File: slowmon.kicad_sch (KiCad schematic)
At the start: 20 parts, among them J801 20021121-00020C4LF, J802 20021121-00020C4LF

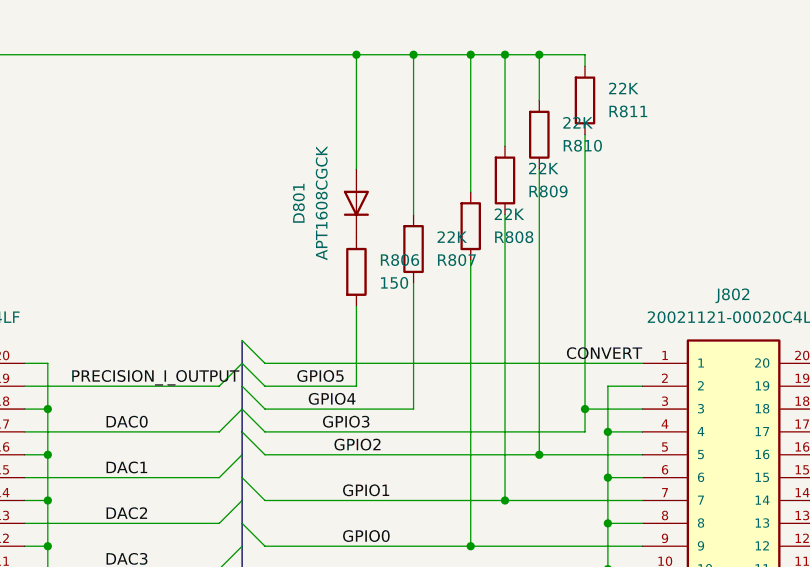
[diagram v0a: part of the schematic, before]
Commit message: Schematic Changes
Added Manufacturer/MPN/Description Fields to parts
Added libraries to project
Modified FMC schematic to use new symbol
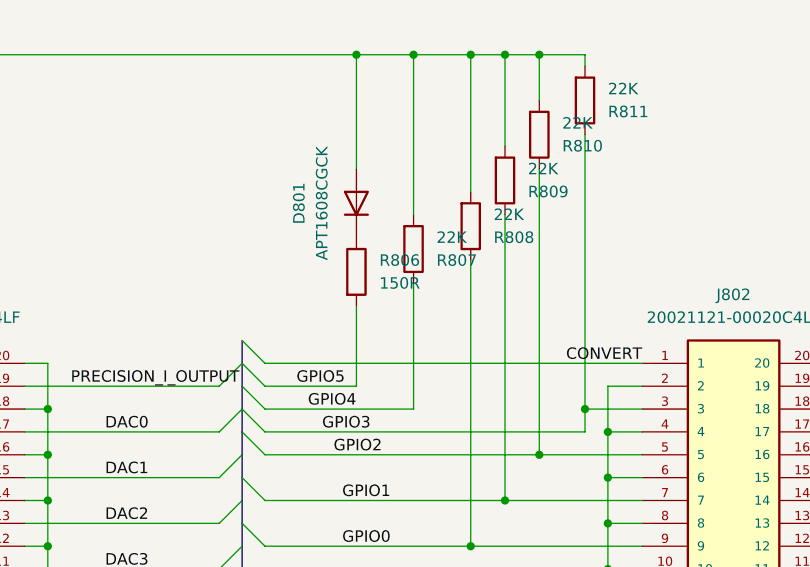
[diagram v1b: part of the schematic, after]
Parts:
- C801: Manufacturer (none) -> Murata; Manufacturer Part Number (none) -> GRM1555C1H221JA01D
- C802, C803, C804, C805, C806: Manufacturer (none) -> Samsung; Manufacturer Part Number (none) -> CL10C151JB8NNNC
- D801: Manufacturer (none) -> Kingbright; Manufacturer Part Number (none) -> APT1608CGCK
- J801, J802: Manufacturer (none) -> Amphenol; Manufacturer Part Number (none) -> 20021121-00020C4LF
- R801, R802, R804: Manufacturer (none) -> YAGEO; Manufacturer Part Number (none) -> RC0603FR-074K75L
- R803, R807, R808, R809, R810, R811: Manufacturer (none) -> YAGEO; Manufacturer Part Number (none) -> RC0603FR-0722KL
- R806: value 150 -> 150R; Manufacturer (none) -> YAGEO; Manufacturer Part Number (none) -> RC0603FR-07150RL

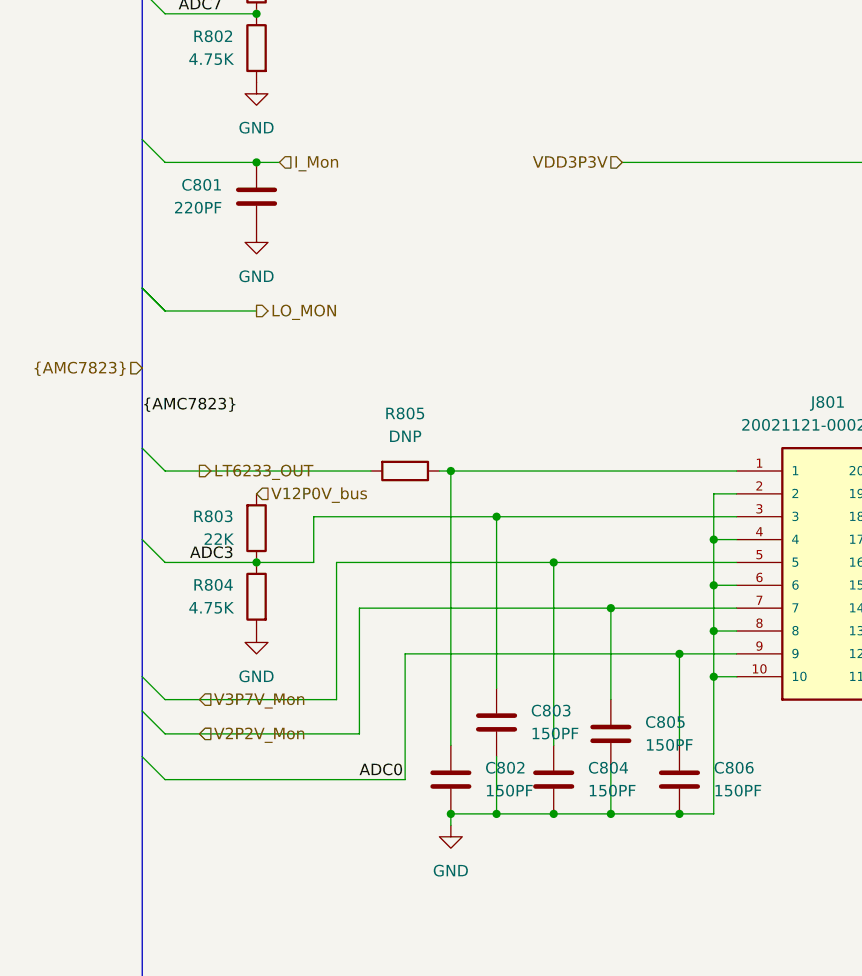
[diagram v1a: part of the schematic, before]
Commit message: Schematics update
Cleaned up RF ADC and front end sections.
Verified that changes did not changes anything about the layout.
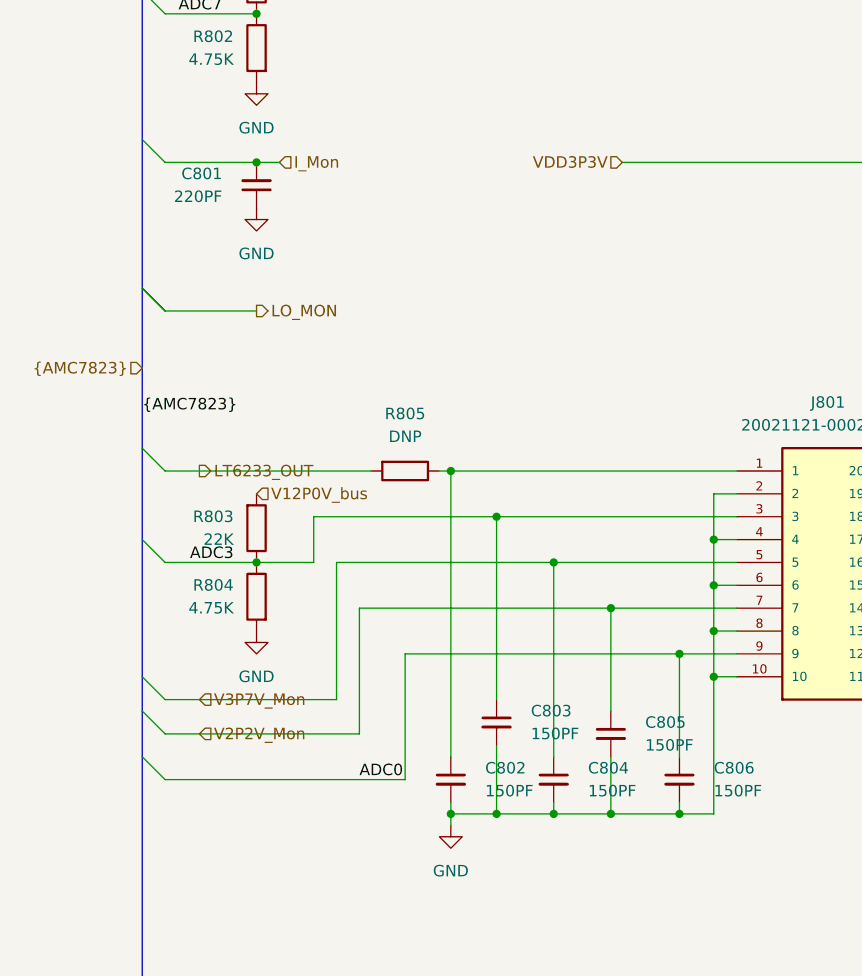
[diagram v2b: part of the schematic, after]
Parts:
- C801, C802, C803, C804, C805, C806: symbol Device:C -> Device:C_Small
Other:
- moved on the sheet: C801
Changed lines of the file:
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@@
 	(paper "A4")
 	(junction
+		(at 100.33 120.65)
+		(diameter 0)
+		(color 0 0 0 0)
+	)
+	(junction
 		(at 104.14 105.41)
 		(diameter 0)
@@
 	)
 	(junction
+		(at 86.36 120.65)
+		(diameter 0)
+		(color 0 0 0 0)
+	)
+	(junction
 		(at 129.54 92.71)
 		(diameter 0)
@@
 	)
 	(junction
+		(at 53.34 48.26)
+		(diameter 0)
+		(color 0 0 0 0)
+	)
+	(junction
 		(at 53.34 31.75)
 		(diameter 0)
@@
 	)
 	(junction
-		(at 53.34 48.26)
-		(diameter 0)
-		(color 0 0 0 0)
-	)
-	(junction
-		(at 100.33 120.65)
-		(diameter 0)
-		(color 0 0 0 0)
-	)
-	(junction
 		(at 180.34 48.26)
 		(diameter 0)
@@
 	)
 	(junction
-		(at 86.36 120.65)
-		(diameter 0)
-		(color 0 0 0 0)
-	)
-	(junction
 		(at 176.53 102.87)
 		(diameter 0)
@@
 	)
 	(junction
-		(at 74.93 120.65)
-		(diameter 0)
-		(color 0 0 0 0)
-	)
-	(junction
 		(at 104.14 95.25)
 		(diameter 0)
@@
 	)
 	(junction
+		(at 74.93 120.65)
+		(diameter 0)
+		(color 0 0 0 0)
+	)
+	(junction
 		(at 53.34 92.71)
 		(diameter 0)
@@
 	(wire
 		(pts
-			(xy 92.71 115.57) (xy 92.71 120.65)
-		)
-		(stroke
-			(width 0)
-			(type default)
-		)
-	)
-	(wire
-		(pts
 			(xy 176.53 48.26) (xy 176.53 63.5)
 		)
@@
 	(wire
 		(pts
+			(xy 92.71 114.3) (xy 92.71 120.65)
+		)
+		(stroke
+			(width 0)
+			(type default)
+		)
+	)
+	(wire
+		(pts
+			(xy 86.36 120.65) (xy 92.71 120.65)
+		)
+		(stroke
+			(width 0)
+			(type default)
+		)
+	)
+	(wire
+		(pts
 			(xy 215.9 102.87) (xy 220.98 102.87)
 		)
@@
 	(wire
 		(pts
+			(xy 74.93 119.38) (xy 74.93 120.65)
+		)
+		(stroke
+			(width 0)
+			(type default)
+		)
+	)
+	(wire
+		(pts
 			(xy 153.67 87.63) (xy 170.18 87.63)
 		)
@@
 	(wire
 		(pts
+			(xy 53.34 48.26) (xy 55.88 48.26)
+		)
+		(stroke
+			(width 0)
+			(type default)
+		)
+	)
+	(wire
+		(pts
 			(xy 62.23 107.95) (xy 62.23 92.71)
 		)
@@
 	(wire
 		(pts
-			(xy 86.36 120.65) (xy 92.71 120.65)
-		)
-		(stroke
-			(width 0)
-			(type default)
-		)
-	)
-	(wire
-		(pts
 			(xy 127 90.17) (xy 148.59 90.17)
 		)
@@
 	(wire
 		(pts
-			(xy 53.34 48.26) (xy 43.18 48.26)
+			(xy 43.18 48.26) (xy 53.34 48.26)
 		)
 		(stroke
@@
 	(wire
 		(pts
+			(xy 100.33 119.38) (xy 100.33 120.65)
+		)
+		(stroke
+			(width 0)
+			(type default)
+		)
+	)
+	(wire
+		(pts
 			(xy 195.58 87.63) (xy 189.23 87.63)
 		)
@@
 		)
 	)
+	(wire
+		(pts
+			(xy 86.36 119.38) (xy 86.36 120.65)
+		)
+		(stroke
+			(width 0)
+			(type default)
+		)
+	)
 	(bus
 		(pts
@@
 	(wire
 		(pts
-			(xy 100.33 120.65) (xy 104.14 120.65)
-		)
-		(stroke
-			(width 0)
-			(type default)
-		)
-	)
-	(wire
-		(pts
 			(xy 104.14 100.33) (xy 104.14 105.41)
 		)
@@
 	(wire
 		(pts
-			(xy 80.01 106.68) (xy 80.01 87.63)
+			(xy 80.01 87.63) (xy 80.01 107.95)
 		)
 		(stroke
@@
 	(wire
 		(pts
-			(xy 55.88 48.26) (xy 53.34 48.26)
-		)
-		(stroke
-			(width 0)
-			(type default)
-		)
-	)
-	(wire
-		(pts
 			(xy 80.01 87.63) (xy 106.68 87.63)
 		)
@@
 		)
 	)
-	(wire
-		(pts
-			(xy 74.93 82.55) (xy 74.93 113.03)
-		)
-		(stroke
-			(width 0)
-			(type default)
-		)
-	)
 	(bus
 		(pts
@@
 	(wire
 		(pts
-			(xy 100.33 113.03) (xy 100.33 102.87)
+			(xy 100.33 102.87) (xy 100.33 114.3)
 		)
 		(stroke
@@
 	(wire
 		(pts
-			(xy 86.36 92.71) (xy 86.36 113.03)
+			(xy 86.36 92.71) (xy 86.36 114.3)
+		)
+		(stroke
+			(width 0)
+			(type default)
+		)
+	)
+	(wire
+		(pts
+			(xy 74.93 82.55) (xy 74.93 114.3)
 		)
 		(stroke
@@
 	(wire
 		(pts
+			(xy 100.33 120.65) (xy 104.14 120.65)
+		)
+		(stroke
+			(width 0)
+			(type default)
+		)
+	)
+	(wire
+		(pts
 			(xy 189.23 90.17) (xy 189.23 87.63)
 		)
@@
 	(wire
 		(pts
-			(xy 80.01 114.3) (xy 80.01 120.65)
+			(xy 80.01 113.03) (xy 80.01 120.65)
 		)
 		(stroke
@@
 	(wire
 		(pts
-			(xy 92.71 97.79) (xy 92.71 107.95)
+			(xy 92.71 97.79) (xy 92.71 109.22)
 		)
 		(stroke
@@
 	)
 	(symbol
-		(lib_id "Device:C")
+		(lib_id "Device:C_Small")
 		(at 74.93 116.84 0)
 		(unit 1)
@@
 	)
 	(symbol
-		(lib_id "Device:C")
+		(lib_id "Device:C_Small")
 		(at 86.36 116.84 0)
 		(unit 1)
@@
 	)
 	(symbol
-		(lib_id "Device:C")
+		(lib_id "Device:C_Small")
 		(at 92.71 111.76 0)
 		(unit 1)
@@
 	)
 	(symbol
-		(lib_id "Device:C")
-		(at 53.34 52.07 0)
+		(lib_id "Device:C_Small")
+		(at 53.34 50.8 0)
 		(mirror x)
 		(unit 1)
@@
 		(fields_autoplaced yes)
 		(property "Reference" "C801"
-			(at 49.53 50.7999 0)
+			(at 49.53 49.5299 0)
 			(effects
 				(font
@@
 		)
 		(property "Value" "220PF"
-			(at 49.53 53.3399 0)
+			(at 49.53 52.0699 0)
 			(effects
 				(font
@@
 		)
 		(property "Footprint" "Capacitor_SMD:C_0402_1005Metric"
-			(at 54.3052 48.26 0)
+			(at 54.3052 46.99 0)
 			(effects
 				(font
@@
 		)
 		(property "Datasheet" "~"
-			(at 53.34 52.07 0)
+			(at 53.34 50.8 0)
 			(effects
 				(font
@@
 		)
 		(property "Description" "CAP CER 220PF 50V C0G/NP0 0402"
-			(at 53.34 52.07 0)
+			(at 53.34 50.8 0)
 			(effects
 				(font
@@
 		)
 		(property "Vendor" "digikey:490-1293-1-ND"
-			(at 0 0 0)
+			(at 0 -1.27 0)
 			(effects
 				(font
@@
 		)
 		(property "Manufacturer" "Murata"
-			(at 53.34 52.07 0)
+			(at 53.34 50.8 0)
 			(effects
 				(font
@@
 		)
 		(property "Manufacturer Part Number" "GRM1555C1H221JA01D"
-			(at 53.34 52.07 0)
+			(at 53.34 50.8 0)
 			(effects
 				(font
@@
 	)
 	(symbol
-		(lib_id "Device:C")
+		(lib_id "Device:C_Small")
 		(at 80.01 110.49 0)
 		(unit 1)
@@
 	(symbol
 		(lib_id "power:GND")
-		(at 53.34 55.88 0)
+		(at 53.34 53.34 0)
 		(mirror y)
 		(unit 1)
@@
 		(fields_autoplaced yes)
 		(property "Reference" "#PWR0802"
-			(at 53.34 62.23 0)
+			(at 53.34 59.69 0)
 			(effects
 				(font
@@
 		)
 		(property "Value" "GND"
-			(at 53.34 60.96 0)
+			(at 53.34 58.42 0)
 			(effects
 				(font
@@
 		)
 		(property "Footprint" ""
-			(at 53.34 55.88 0)
+			(at 53.34 53.34 0)
 			(effects
 				(font
@@
 		)
 		(property "Datasheet" ""
-			(at 53.34 55.88 0)
+			(at 53.34 53.34 0)
 			(effects
 				(font
@@
 		)
 		(property "Description" "Power symbol creates a global label with name \"GND\" , ground"
-			(at 53.34 55.88 0)
+			(at 53.34 53.34 0)
 			(effects
 				(font
@@
 	)
 	(symbol
-		(lib_id "Device:C")
+		(lib_id "Device:C_Small")
 		(at 100.33 116.84 0)
 		(unit 1)

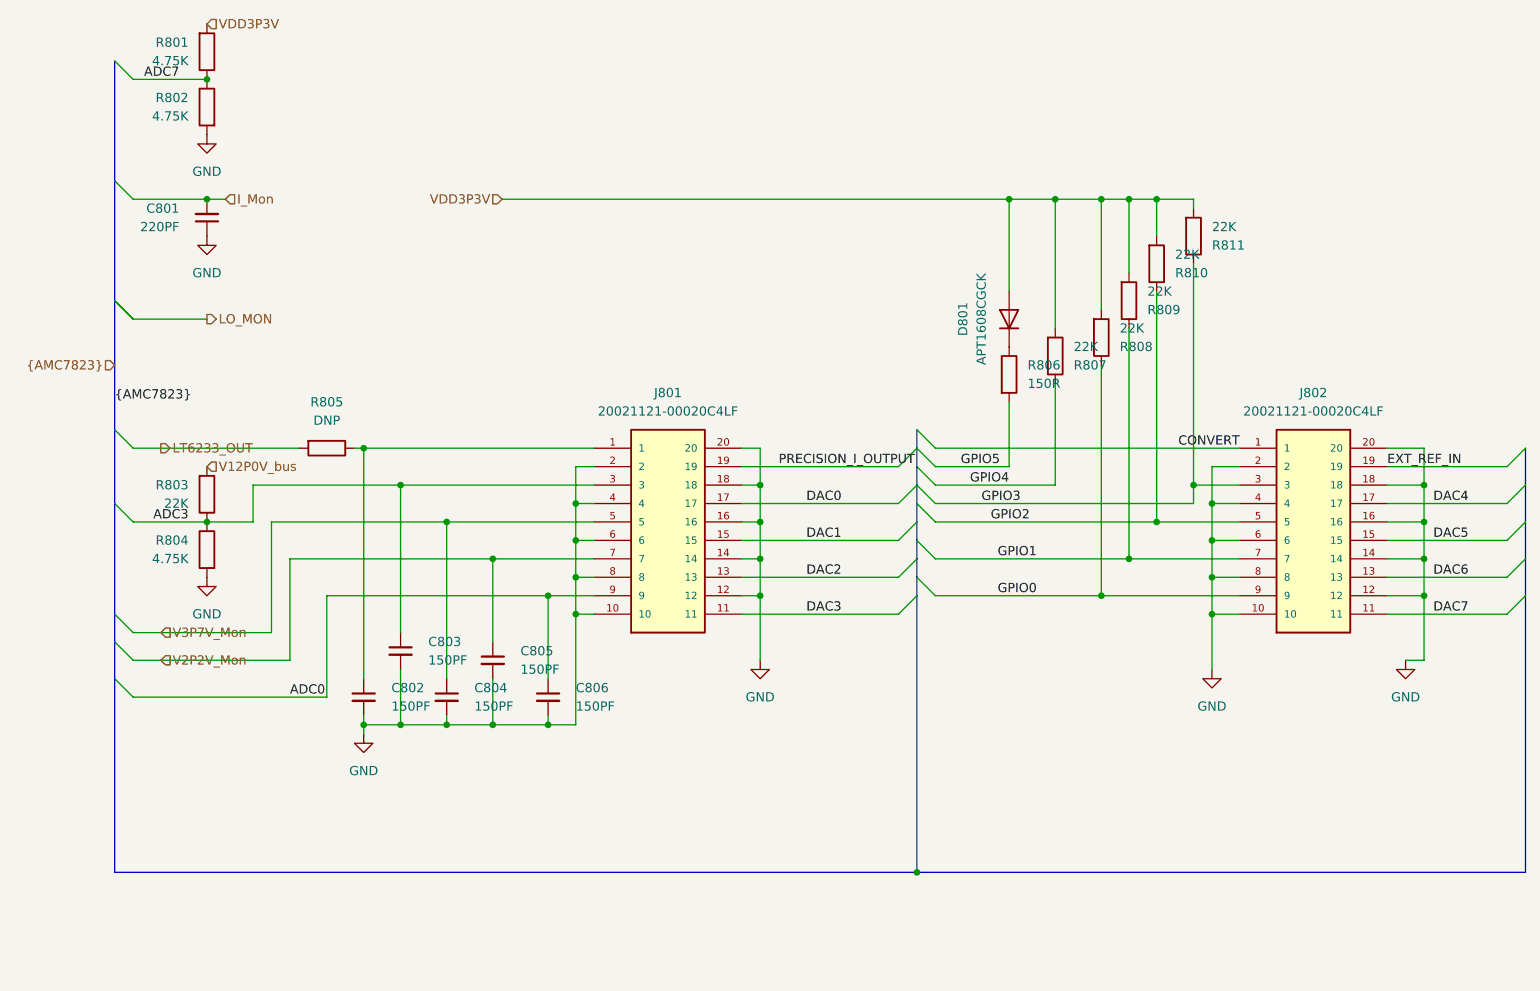
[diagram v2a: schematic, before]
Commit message: Updated some Schematics
- updated slowmon schematic
- updated diff to se schematic
- cleaned up DRC/ERC errors
No changes were made that effected the PCB layout
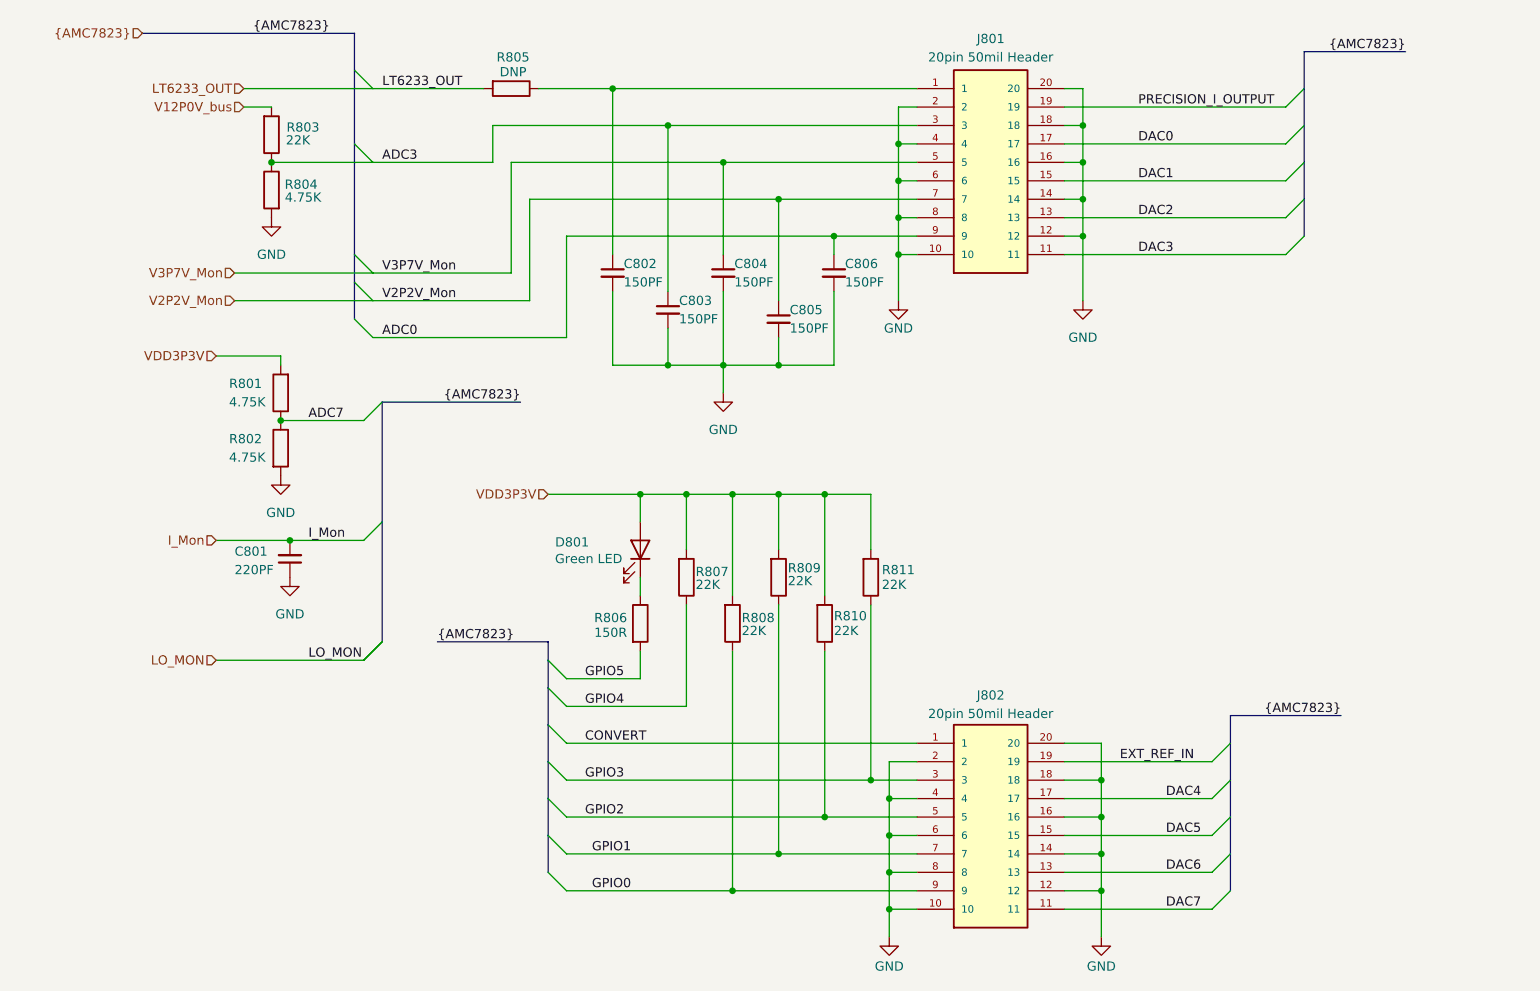
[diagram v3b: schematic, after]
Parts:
- D801: value APT1608CGCK -> Green LED; symbol Device:D -> Device:LED
- J801, J802: value 20021121-00020C4LF -> 20pin 50mil Header
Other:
- moved on the sheet: C801, C802, C803, C804, C805, C806, J801, J802, R801, R802, R803, R804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

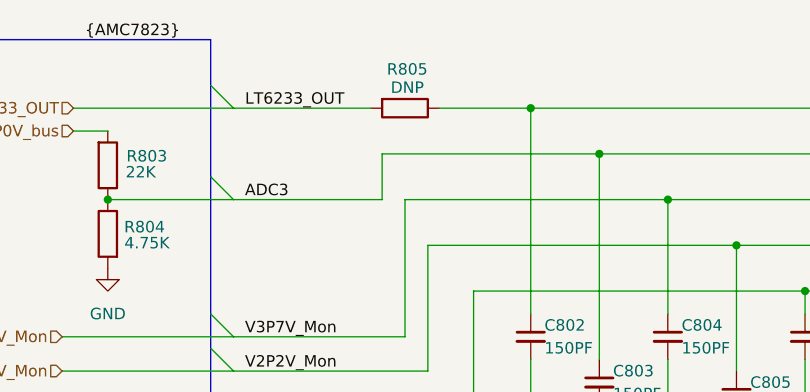
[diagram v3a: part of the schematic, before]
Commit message: Properly attributed DNP parts; Added Fabrication Notes
-Properly attributed various DNP in the project;
This includes: C210.C710,C1601,C2502,C2602,L2501,R1507,L2601,R1601,R805
- I changed the accelerometer and microphone (+it's filter)to DNP parts
  Note: both of these are obsolete parts. As part of this change I Changed R1602 (part of mic buffer) from 220k to 0R. The removal of these parts should in no way negatively effect the rest of the circuit.
-I fixed the 'value' attribute of XMER2501&XMER2601 from 'TC4-6+' -> 'TC4-6T+'
- I added some fabrication notes to the F.Fab Layer
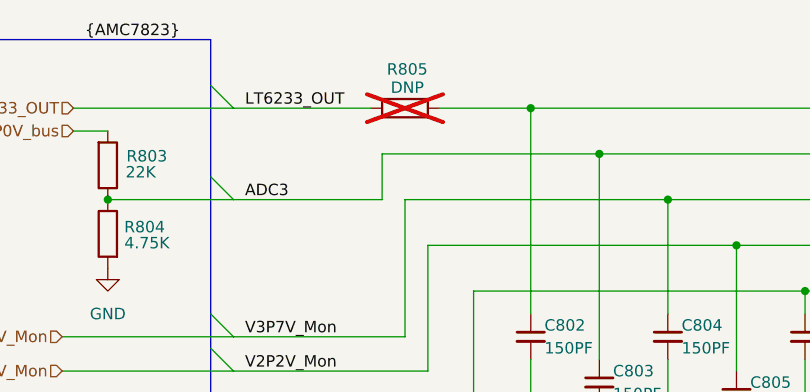
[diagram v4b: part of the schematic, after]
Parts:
- R805: now not fitted
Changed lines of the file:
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@@
 		(in_bom yes)
 		(on_board yes)
-		(dnp no)
+		(dnp yes)
 		(property "Reference" "R805"
 			(at 95.504 28.702 90)
